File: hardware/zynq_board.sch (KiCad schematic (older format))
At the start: 0 parts

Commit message: WIP: routing the HF Part of the Camera Connector. I have to move the clock away from the left border.
TODO: Fix DDR3 RAM.
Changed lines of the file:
@@
 F1 "pmic.sch" 60
 F2 "PS_POR_B" O R 6500 6700 60
-F3 "V_IN" I R 6500 5950 60
 $EndSheet
 $Sheet
@@
 F0 "DDR" 60
 F1 "ddr.sch" 60
-$EndSheet
-$Sheet
-S 23600 16850 2100 1100
-U 597B38C9
-F0 "10G Clock" 60
-F1 "10G_clock.sch" 60
-F2 "156_25_MHZ_0_P" O L 23600 16950 60
-F3 "156_25_MHZ_0_N" O L 23600 17050 60
-F4 "125_00_MHZ_P" O L 23600 17250 60
-F5 "125_00_MHZ_N" O L 23600 17350 60
-F6 "156_25_MHZ_1_P" O L 23600 17550 60
-F7 "156_25_MHZ_1_N" O L 23600 17650 60
 $EndSheet
 $Sheet
@@
 F13 "CLK" O R 6500 9750 60
 F14 "VBUS_FAULT" O R 6500 10050 60
-F15 "RESETB" I R 6500 9950 60
 $EndSheet
 $Sheet
@@
 F7 "MGTX_RX_1_P" I R 13250 19050 60
 F8 "MGTX_RX_2_P" I R 13250 18950 60
-F9 "MGTREFCLK_0_N" I R 13250 18450 60
-F10 "MGTREFCLK_0_P" I R 13250 18350 60
-F11 "MGTREFCLK_1_N" I R 13250 18700 60
-F12 "MGTREFCLK_1_P" I R 13250 18600 60
-F13 "MGTX_RX_3_P" I R 13250 18850 60
-F14 "MGTX_TX_0_P" O R 13250 20100 60
-F15 "MGTX_TX_1_P" O R 13250 20000 60
-F16 "MGTX_TX_2_P" O R 13250 19900 60
-F17 "MGTX_TX_3_P" O R 13250 19800 60
-F18 "MGTX_TX_0_N" O R 13250 20550 60
-F19 "MGTX_TX_1_N" O R 13250 20450 60
-F20 "MGTX_TX_2_N" O R 13250 20350 60
-F21 "MGTX_TX_3_N" O R 13250 20250 60
+F9 "MGTX_RX_3_P" I R 13250 18850 60
+F10 "MGTX_TX_0_P" O R 13250 20100 60
+F11 "MGTX_TX_1_P" O R 13250 20000 60
+F12 "MGTX_TX_2_P" O R 13250 19900 60
+F13 "MGTX_TX_3_P" O R 13250 19800 60
+F14 "MGTX_TX_0_N" O R 13250 20550 60
+F15 "MGTX_TX_1_N" O R 13250 20450 60
+F16 "MGTX_TX_2_N" O R 13250 20350 60
+F17 "MGTX_TX_3_N" O R 13250 20250 60
 $EndSheet
 $Sheet
@@
 F8 "INA[0]_P" I L 23600 20100 60
 F9 "INA[0]_N" I L 23600 20550 60
-F10 "REFCLK0_P" I L 23600 18550 60
-F11 "REFCLK0_N" I L 23600 18650 60
-F12 "HSRXA_P" I R 25700 18550 60
-F13 "HSRXA_N" I R 25700 18650 60
-F14 "MDC" I R 25700 20950 60
-F15 "LS_OK_IN_A" I R 25700 20550 60
-F16 "LS_OK_OUT_A" O R 25700 20650 60
-F17 "ST" I R 25700 20400 60
-F18 "PRBSEN" I R 25700 20800 60
-F19 "MDIO" B R 25700 21050 60
-F20 "OUTA[3]_P" O L 23600 18850 60
-F21 "OUTA[3]_N" O L 23600 19300 60
-F22 "OUTA[2]_P" O L 23600 18950 60
-F23 "OUTA[2]_N" O L 23600 19400 60
-F24 "OUTA[1]_P" O L 23600 19050 60
-F25 "OUTA[1]_N" O L 23600 19500 60
-F26 "OUTA[0]_P" O L 23600 19150 60
-F27 "OUTA[0]_N" O L 23600 19600 60
-F28 "HSTXA_P" O R 25700 18800 60
-F29 "HSTXA_N" O R 25700 18900 60
-F30 "~TLK_RESET~" I R 25700 21200 60
+F10 "HSRXA_P" I R 25700 18550 60
+F11 "HSRXA_N" I R 25700 18650 60
+F12 "MDC" I R 25700 20950 60
+F13 "LS_OK_IN_A" I R 25700 20550 60
+F14 "LS_OK_OUT_A" O R 25700 20650 60
+F15 "ST" I R 25700 20400 60
+F16 "PRBSEN" I R 25700 20800 60
+F17 "MDIO" B R 25700 21050 60
+F18 "OUTA[3]_P" O L 23600 18850 60
+F19 "OUTA[3]_N" O L 23600 19300 60
+F20 "OUTA[2]_P" O L 23600 18950 60
+F21 "OUTA[2]_N" O L 23600 19400 60
+F22 "OUTA[1]_P" O L 23600 19050 60
+F23 "OUTA[1]_N" O L 23600 19500 60
+F24 "OUTA[0]_P" O L 23600 19150 60
+F25 "OUTA[0]_N" O L 23600 19600 60
+F26 "HSTXA_P" O R 25700 18800 60
+F27 "HSTXA_N" O R 25700 18900 60
 $EndSheet
 $Sheet
@@
 	13450 22250 13450 2650
 Wire Wire Line
-	13250 18350 22700 18350
-Wire Wire Line
-	22700 18350 22700 16950
-Wire Wire Line
-	22700 16950 23600 16950
-Wire Wire Line
-	23600 17050 22800 17050
-Wire Wire Line
-	22800 17050 22800 18450
-Wire Wire Line
-	22800 18450 13250 18450
-Wire Wire Line
-	13250 18600 23000 18600
-Wire Wire Line
-	23000 18600 23000 17250
-Wire Wire Line
-	23000 17250 23600 17250
-Wire Wire Line
-	13250 18700 23100 18700
-Wire Wire Line
-	23100 18700 23100 17350
-Wire Wire Line
-	23100 17350 23600 17350
-Wire Wire Line
-	23600 17550 23500 17550
-Wire Wire Line
-	23500 17550 23500 18550
-Wire Wire Line
-	23500 18550 23600 18550
-Wire Wire Line
-	23600 17650 23400 17650
-Wire Wire Line
-	23400 17650 23400 18650
-Wire Wire Line
-	23400 18650 23600 18650
-Wire Wire Line
 	13250 18850 23600 18850
 Wire Wire Line
@@
 Wire Wire Line
 	25700 21050 26550 21050
-Wire Wire Line
-	25700 21200 26550 21200
 Text Label 26550 20550 2    60   ~ 0
 LS_OK_IN_A
@@
 Text Label 26550 21050 2    60   ~ 0
 MDIO
-Text Label 26550 21200 2    60   ~ 0
-~TLK_RESET~
 Wire Wire Line
 	13250 5100 14100 5100
@@
 Wire Wire Line
 	13250 4600 14100 4600
-Wire Wire Line
-	13250 4500 14100 4500
 Text Label 14100 5000 2    60   ~ 0
 LS_OK_IN_A
@@
 Text Label 14100 4600 2    60   ~ 0
 MDIO
-Text Label 14100 4500 2    60   ~ 0
-~TLK_RESET~
 Wire Wire Line
 	19600 6600 20500 6600
@@
 Text Label 14150 4300 2    60   ~ 0
 IMU_INT2_GPIO2
+Text Label 7200 9950 0    60   ~ 0
+PG
+Wire Wire Line
+	7450 9950 7200 9950
+Text Label 6800 6700 2    60   ~ 0
+PG
+Wire Wire Line
+	6800 6700 6500 6700
+Text Label 13800 8550 2    60   ~ 0
+IMU_MISO
+Wire Wire Line
+	13250 8550 13800 8550
+Text Label 13800 8650 2    60   ~ 0
+IMU_MOSI
+Wire Wire Line
+	13250 8650 13800 8650
+Text Label 13800 8900 2    60   ~ 0
+IMU_EN_0
+Wire Wire Line
+	13250 8900 13800 8900
+Text Label 13800 9000 2    60   ~ 0
+IMU_EN_1
+Wire Wire Line
+	13250 9000 13800 9000
+Text Label 13800 8750 2    60   ~ 0
+IMU_CLK
+Wire Wire Line
+	13250 8750 13800 8750
+Text Label 17350 8550 0    60   ~ 0
+IMU_MISO
+Wire Wire Line
+	17900 8550 17350 8550
+Text Label 17350 8650 0    60   ~ 0
+IMU_MOSI
+Wire Wire Line
+	17900 8650 17350 8650
+Text Label 17350 8900 0    60   ~ 0
+IMU_EN_0
+Wire Wire Line
+	17900 8900 17350 8900
+Text Label 17350 9000 0    60   ~ 0
+IMU_EN_1
+Wire Wire Line
+	17900 9000 17350 9000
+Text Label 17350 8750 0    60   ~ 0
+IMU_CLK
+Wire Wire Line
+	17900 8750 17350 8750
+Text Label 14450 8500 0    60   ~ 0
+LED1
+Text Label 14450 8600 0    60   ~ 0
+LED2
+Wire Wire Line
+	14950 8500 14450 8500
+Wire Wire Line
+	14950 8600 14450 8600
+$Sheet
+S 5000 3200 1500 1150
+U 5AFB0E10
+F0 "Power Connector, Protection" 60
+F1 "pwr_con_fuse_filter.sch" 60
+$EndSheet
 $Sheet
 S 10500 2550 2750 3550
@@
 F18 "TXD" O R 13250 3950 60
 F19 "~SBA~" O R 13250 3650 60
-F20 "~TLK_RESET~" O R 13250 4500 60
-F21 "GPIO_9" B R 13250 2650 60
-F22 "GPIO_10" B R 13250 2750 60
-F23 "GPIO_11" B R 13250 2850 60
-F24 "GPIO_12" B R 13250 2950 60
-F25 "GPIO_13" B R 13250 3050 60
-F26 "GPIO_14" B R 13250 3150 60
-F27 "GPIO_15" B R 13250 3250 60
-F28 "IMU_FRAME_GPIO0" O R 13250 4100 60
-F29 "IMU_INT1_GPIO1" I R 13250 4200 60
-F30 "IMU_INT0_GPIO2" I R 13250 4300 60
-$EndSheet
-Text Label 7200 9950 0    60   ~ 0
-PG
-Wire Wire Line
-	7450 9950 7200 9950
-Text Label 6800 6700 2    60   ~ 0
-PG
-Wire Wire Line
-	6800 6700 6500 6700
-Text Label 13800 8550 2    60   ~ 0
-IMU_MISO
-Wire Wire Line
-	13250 8550 13800 8550
-Text Label 13800 8650 2    60   ~ 0
-IMU_MOSI
-Wire Wire Line
-	13250 8650 13800 8650
-Text Label 13800 8900 2    60   ~ 0
-IMU_EN_0
-Wire Wire Line
-	13250 8900 13800 8900
-Text Label 13800 9000 2    60   ~ 0
-IMU_EN_1
-Wire Wire Line
-	13250 9000 13800 9000
-Text Label 13800 8750 2    60   ~ 0
-IMU_CLK
-Wire Wire Line
-	13250 8750 13800 8750
-Text Label 17350 8550 0    60   ~ 0
-IMU_MISO
-Wire Wire Line
-	17900 8550 17350 8550
-Text Label 17350 8650 0    60   ~ 0
-IMU_MOSI
-Wire Wire Line
-	17900 8650 17350 8650
-Text Label 17350 8900 0    60   ~ 0
-IMU_EN_0
-Wire Wire Line
-	17900 8900 17350 8900
-Text Label 17350 9000 0    60   ~ 0
-IMU_EN_1
-Wire Wire Line
-	17900 9000 17350 9000
-Text Label 17350 8750 0    60   ~ 0
-IMU_CLK
-Wire Wire Line
-	17900 8750 17350 8750
-Text Label 14450 8500 0    60   ~ 0
-LED1
-Text Label 14450 8600 0    60   ~ 0
-LED2
-Wire Wire Line
-	14950 8500 14450 8500
-Wire Wire Line
-	14950 8600 14450 8600
-$Sheet
-S 5000 3200 1500 1150
-U 5AFB0E10
-F0 "Power Connector, Protection" 60
-F1 "pwr_con_fuse_filter.sch" 60
-F2 "V_IN" O R 6500 3800 60
-$EndSheet
-Wire Wire Line
-	6500 3800 6800 3800
-Text Label 6800 3800 2    60   ~ 0
-V_IN
-Wire Wire Line
-	6500 5950 6800 5950
-Text Label 6800 5950 2    60   ~ 0
-V_IN
+F20 "GPIO_9" B R 13250 2650 60
+F21 "GPIO_10" B R 13250 2750 60
+F22 "GPIO_11" B R 13250 2850 60
+F23 "GPIO_12" B R 13250 2950 60
+F24 "GPIO_13" B R 13250 3050 60
+F25 "GPIO_14" B R 13250 3150 60
+F26 "GPIO_15" B R 13250 3250 60
+F27 "IMU_FRAME_GPIO0" O R 13250 4100 60
+F28 "IMU_INT1_GPIO1" I R 13250 4200 60
+F29 "IMU_INT0_GPIO2" I R 13250 4300 60
+$EndSheet
+$Sheet
+S 23600 16850 2100 1100
+U 597B38C9
+F0 "10G Clock" 60
+F1 "10G_clock.sch" 60
+$EndSheet
 $EndSCHEMATC

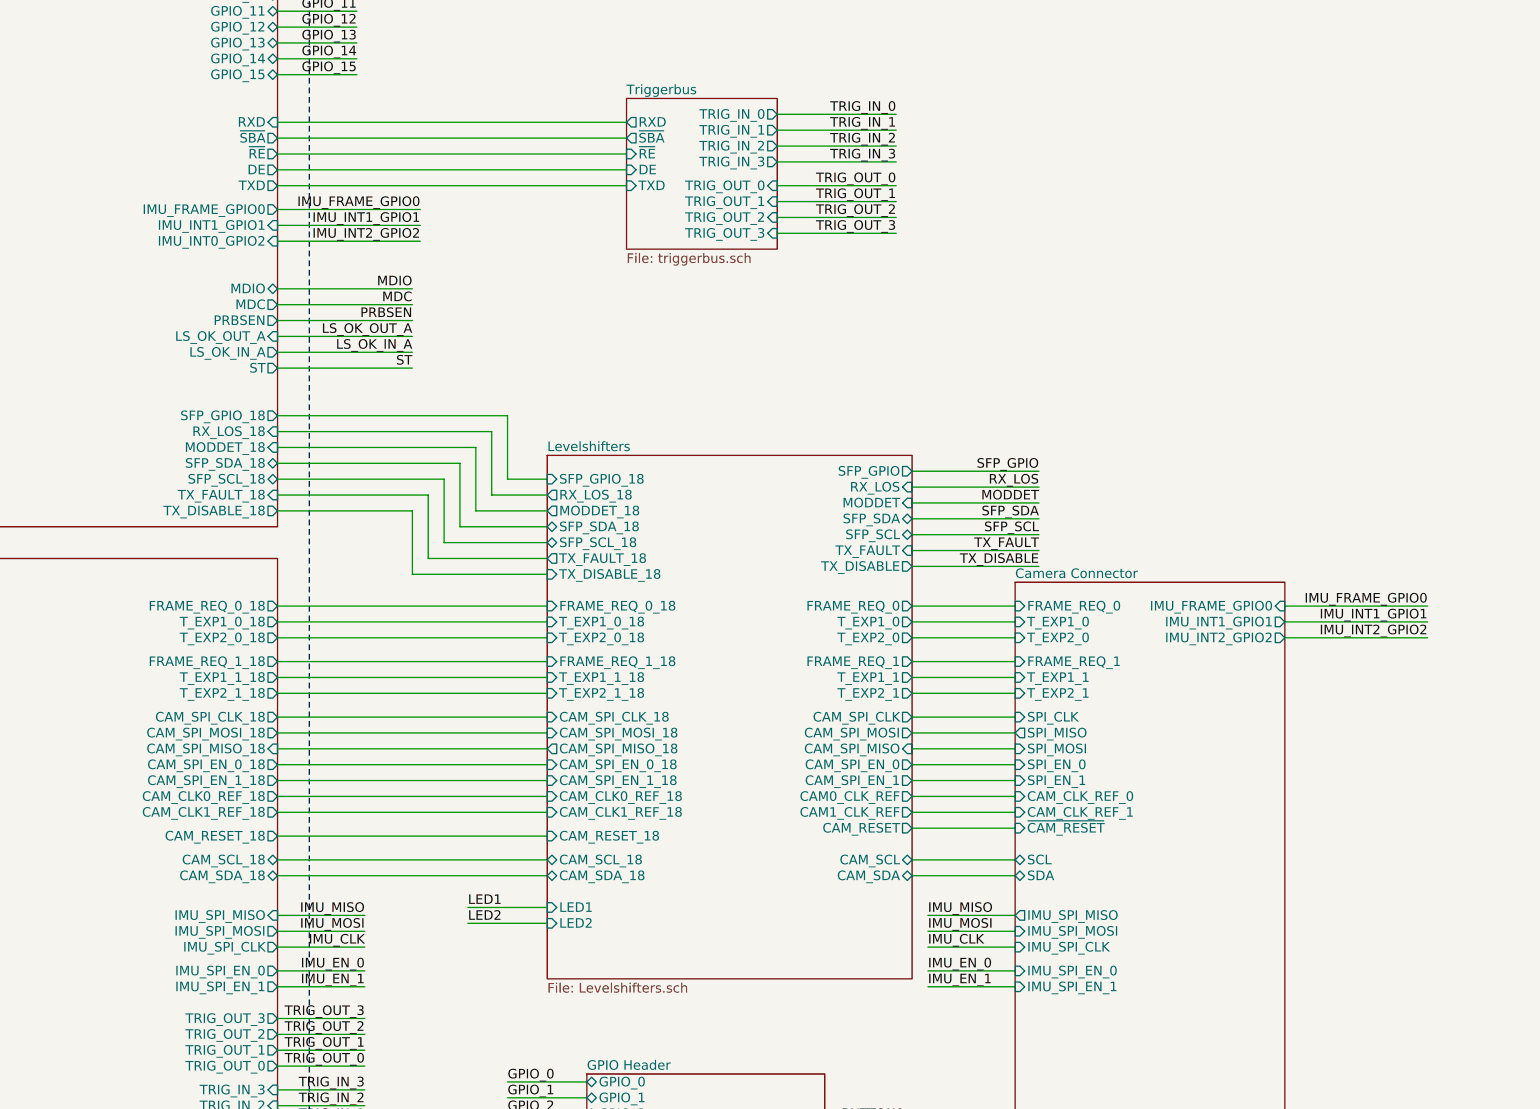
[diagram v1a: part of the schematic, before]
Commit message: Added Courtyard to selfmade Footprints. Also general Routing WIP.
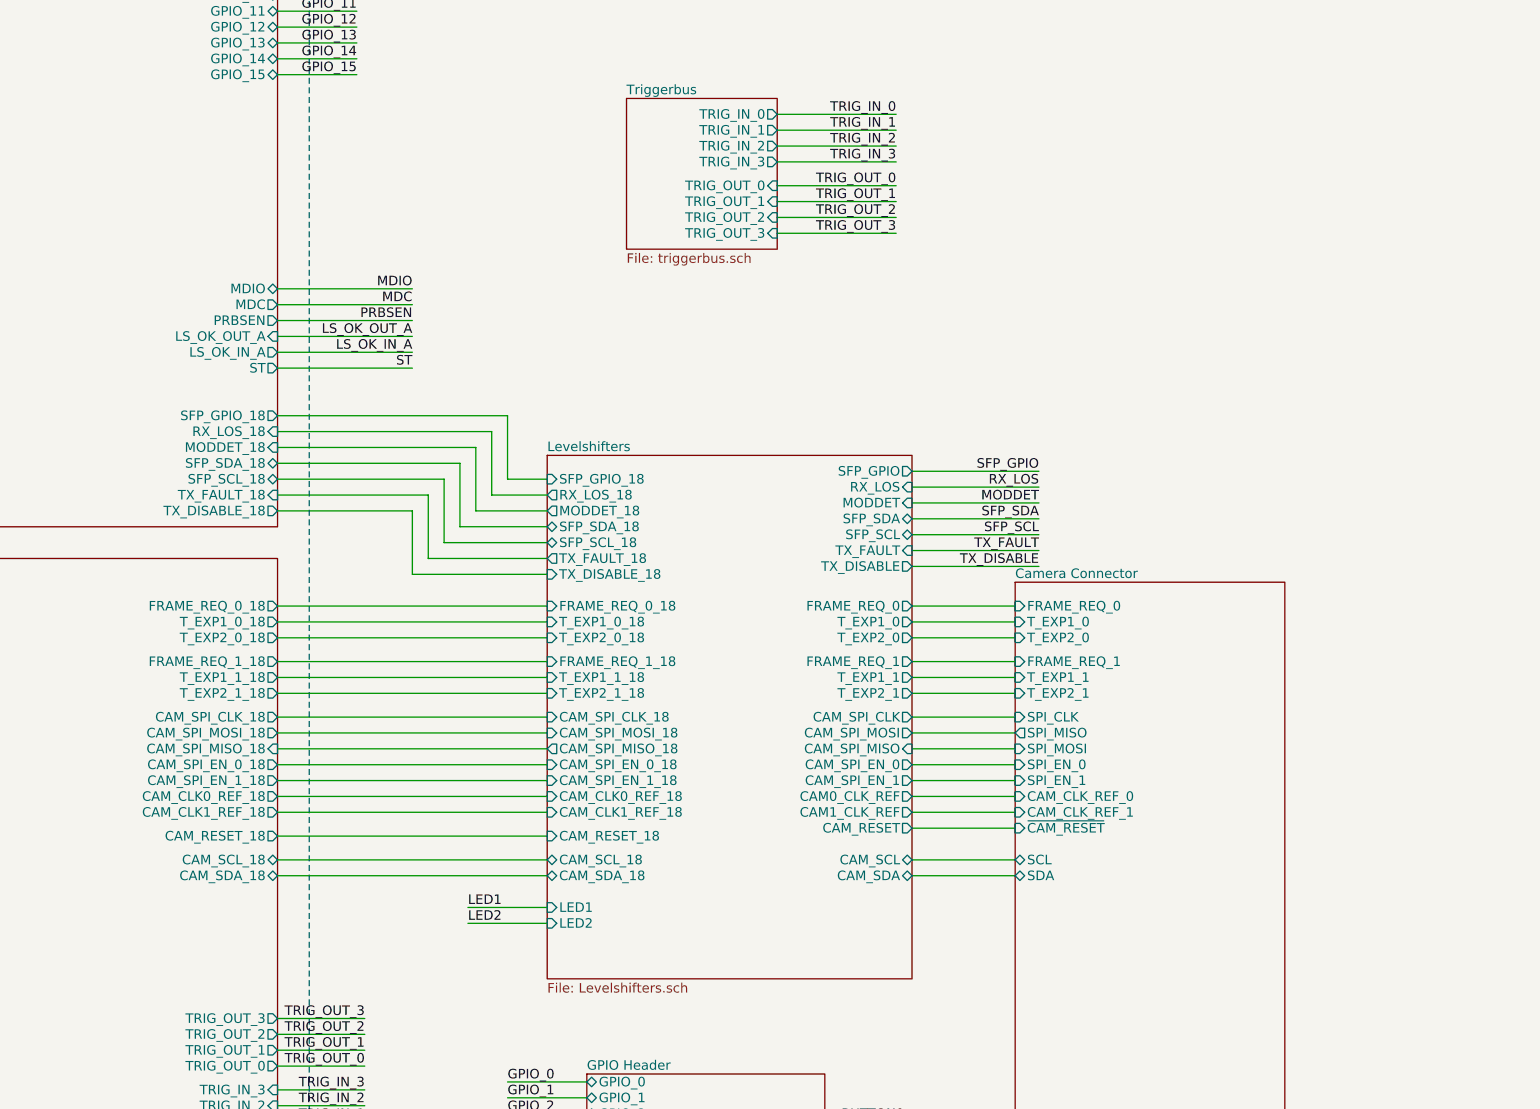
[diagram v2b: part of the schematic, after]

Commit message: WIP: general Routing
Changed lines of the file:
@@
 F21 "CAM_RESET" O R 17250 8000 60
 F22 "CAM_SPI_EN_0" O R 17250 7600 60
-F23 "CAM_SCL_18" B L 14950 8200 60
-F24 "CAM_SDA_18" B L 14950 8300 60
-F25 "SFP_SCL_18" B L 14950 6200 60
-F26 "SFP_SDA_18" B L 14950 6100 60
-F27 "CAM_RESET_18" I L 14950 8050 60
-F28 "CAM_SPI_EN_1_18" I L 14950 7700 60
-F29 "CAM_SPI_EN_0_18" I L 14950 7600 60
-F30 "CAM_SPI_MOSI_18" I L 14950 7400 60
-F31 "CAM_SPI_CLK_18" I L 14950 7300 60
-F32 "T_EXP2_1_18" I L 14950 7150 60
-F33 "T_EXP1_1_18" I L 14950 7050 60
-F34 "FRAME_REQ_1_18" I L 14950 6950 60
-F35 "T_EXP2_0_18" I L 14950 6800 60
-F36 "T_EXP1_0_18" I L 14950 6700 60
-F37 "FRAME_REQ_0_18" I L 14950 6600 60
-F38 "CAM_SPI_MISO_18" O L 14950 7500 60
-F39 "RX_LOS_18" O L 14950 5900 60
-F40 "TX_FAULT_18" O L 14950 6300 60
-F41 "MODDET_18" O L 14950 6000 60
-F42 "SFP_GPIO_18" I L 14950 5800 60
-F43 "TX_DISABLE_18" I L 14950 6400 60
-F44 "CAM1_CLK_REF" O R 17250 7900 60
-F45 "CAM_CLK1_REF_18" I L 14950 7900 60
-F46 "CAM_CLK0_REF_18" I L 14950 7800 60
-F47 "CAM0_CLK_REF" O R 17250 7800 60
-F48 "LED1" I L 14950 8500 60
-F49 "LED2" I L 14950 8600 60
+F23 "SFP_SCL_18" B L 14950 6200 60
+F24 "SFP_SDA_18" B L 14950 6100 60
+F25 "CAM_RESET_18" I L 14950 8050 60
+F26 "CAM_SPI_EN_1_18" I L 14950 7700 60
+F27 "CAM_SPI_EN_0_18" I L 14950 7600 60
+F28 "CAM_SPI_MOSI_18" I L 14950 7400 60
+F29 "CAM_SPI_CLK_18" I L 14950 7300 60
+F30 "T_EXP2_1_18" I L 14950 7150 60
+F31 "T_EXP1_1_18" I L 14950 7050 60
+F32 "FRAME_REQ_1_18" I L 14950 6950 60
+F33 "T_EXP2_0_18" I L 14950 6800 60
+F34 "T_EXP1_0_18" I L 14950 6700 60
+F35 "FRAME_REQ_0_18" I L 14950 6600 60
+F36 "CAM_SPI_MISO_18" O L 14950 7500 60
+F37 "RX_LOS_18" O L 14950 5900 60
+F38 "TX_FAULT_18" O L 14950 6300 60
+F39 "MODDET_18" O L 14950 6000 60
+F40 "SFP_GPIO_18" I L 14950 5800 60
+F41 "TX_DISABLE_18" I L 14950 6400 60
+F42 "CAM1_CLK_REF" O R 17250 7900 60
+F43 "CAM_CLK1_REF_18" I L 14950 7900 60
+F44 "CAM_CLK0_REF_18" I L 14950 7800 60
+F45 "CAM0_CLK_REF" O R 17250 7800 60
+F46 "LED1" I L 14950 8500 60
+F47 "LED2" I L 14950 8600 60
 $EndSheet
 $Sheet
@@
 Text Label 17150 3800 2    60   ~ 0
 TRIG_IN_3
-Text Label 13750 10100 2    60   ~ 0
-GPIO_0
-Text Label 13750 10200 2    60   ~ 0
-GPIO_1
-Text Label 13750 10300 2    60   ~ 0
-GPIO_2
-Text Label 13750 10400 2    60   ~ 0
-GPIO_3
-Text Label 13750 10500 2    60   ~ 0
-GPIO_4
-Text Label 13750 10600 2    60   ~ 0
-GPIO_5
-Text Label 13750 10700 2    60   ~ 0
-GPIO_6
-Text Label 13750 10800 2    60   ~ 0
-GPIO_7
-Text Label 13750 10900 2    60   ~ 0
-GPIO_8
 Text Label 13750 3250 2    60   ~ 0
 GPIO_15
@@
 Wire Wire Line
 	13250 8050 14950 8050
-Wire Wire Line
-	14950 8200 13250 8200
-Wire Wire Line
-	13250 8300 14950 8300
 Wire Notes Line
 	13450 2350 7250 2350
@@
 Wire Wire Line
 	13250 3250 13750 3250
-Wire Wire Line
-	13250 10100 13750 10100
-Wire Wire Line
-	13250 10200 13750 10200
-Wire Wire Line
-	13250 10300 13750 10300
-Wire Wire Line
-	13250 10400 13750 10400
-Wire Wire Line
-	13250 10500 13750 10500
-Wire Wire Line
-	13250 10600 13750 10600
-Wire Wire Line
-	13250 10700 13750 10700
-Wire Wire Line
-	13250 10800 13750 10800
-Wire Wire Line
-	13250 10900 13750 10900
-$Sheet
-S 15200 9550 1500 1700
-U 5B0F4BF9
-F0 "GPIO Header" 60
-F1 "gpio.sch" 60
-F2 "GPIO_0" B L 15200 9600 60
-F3 "GPIO_1" B L 15200 9700 60
-F4 "GPIO_2" B L 15200 9800 60
-F5 "GPIO_3" B L 15200 9900 60
-F6 "GPIO_4" B L 15200 10000 60
-F7 "GPIO_5" B L 15200 10100 60
-F8 "GPIO_6" B L 15200 10200 60
-F9 "GPIO_7" B L 15200 10300 60
-F10 "GPIO_8" B L 15200 10400 60
-F11 "GPIO_9" B L 15200 10500 60
-F12 "GPIO_10" B L 15200 10600 60
-F13 "GPIO_11" B L 15200 10700 60
-F14 "GPIO_12" B L 15200 10800 60
-F15 "GPIO_13" B L 15200 10900 60
-F16 "GPIO_14" B L 15200 11000 60
-F17 "GPIO_15" B L 15200 11100 60
-F18 "BUTTON1" O R 16700 9850 60
-$EndSheet
-Text Label 14700 9600 0    60   ~ 0
-GPIO_0
-Wire Wire Line
-	14700 9600 15200 9600
-Text Label 14700 9700 0    60   ~ 0
-GPIO_1
-Wire Wire Line
-	14700 9700 15200 9700
-Text Label 14700 9800 0    60   ~ 0
-GPIO_2
-Wire Wire Line
-	14700 9800 15200 9800
-Text Label 14700 9900 0    60   ~ 0
-GPIO_3
-Wire Wire Line
-	14700 9900 15200 9900
-Text Label 14700 10000 0    60   ~ 0
-GPIO_4
-Wire Wire Line
-	14700 10000 15200 10000
-Text Label 14700 10100 0    60   ~ 0
-GPIO_5
-Wire Wire Line
-	14700 10100 15200 10100
-Text Label 14700 10200 0    60   ~ 0
-GPIO_6
-Wire Wire Line
-	14700 10200 15200 10200
-Text Label 14700 10300 0    60   ~ 0
-GPIO_7
-Wire Wire Line
-	14700 10300 15200 10300
-Text Label 14700 10400 0    60   ~ 0
-GPIO_8
-Wire Wire Line
-	14700 10400 15200 10400
-Text Label 14700 10500 0    60   ~ 0
-GPIO_9
-Wire Wire Line
-	14700 10500 15200 10500
-Text Label 14700 10600 0    60   ~ 0
-GPIO_10
-Wire Wire Line
-	14700 10600 15200 10600
-Text Label 14700 10700 0    60   ~ 0
-GPIO_11
-Wire Wire Line
-	14700 10700 15200 10700
-Text Label 14700 10800 0    60   ~ 0
-GPIO_12
-Wire Wire Line
-	14700 10800 15200 10800
-Text Label 14700 10900 0    60   ~ 0
-GPIO_13
-Wire Wire Line
-	14700 10900 15200 10900
-Text Label 14700 11000 0    60   ~ 0
-GPIO_14
-Wire Wire Line
-	14700 11000 15200 11000
-Text Label 14700 11100 0    60   ~ 0
-GPIO_15
-Wire Wire Line
-	14700 11100 15200 11100
 Text Label 13750 11150 2    60   ~ 0
 LED1
@@
 F12 "CAM_SPI_EN_0_18" O R 13250 7600 60
 F13 "CAM_RESET_18" O R 13250 8050 60
-F14 "CAM_SCL_18" B R 13250 8200 60
-F15 "CAM_SDA_18" B R 13250 8300 60
-F16 "TRIG_IN_0" I R 13250 9950 60
-F17 "TRIG_IN_1" I R 13250 9850 60
-F18 "TRIG_IN_2" I R 13250 9750 60
-F19 "TRIG_IN_3" I R 13250 9650 60
-F20 "TRIG_OUT_0" O R 13250 9500 60
-F21 "TRIG_OUT_2" O R 13250 9300 60
-F22 "TRIG_OUT_1" O R 13250 9400 60
-F23 "TRIG_OUT_3" O R 13250 9200 60
-F24 "GPIO_0" B R 13250 10100 60
-F25 "GPIO_1" B R 13250 10200 60
-F26 "GPIO_2" B R 13250 10300 60
-F27 "GPIO_3" B R 13250 10400 60
-F28 "GPIO_4" B R 13250 10500 60
-F29 "GPIO_5" B R 13250 10600 60
-F30 "GPIO_6" B R 13250 10700 60
-F31 "GPIO_7" B R 13250 10800 60
-F32 "GPIO_8" B R 13250 10900 60
-F33 "LED1" O R 13250 11150 60
-F34 "LED2" O R 13250 11250 60
-F35 "BUTTON0" I R 13250 11350 60
-F36 "CAM_CLK0_REF_18" O R 13250 7800 60
-F37 "CAM_CLK1_REF_18" O R 13250 7900 60
+F14 "TRIG_IN_0" I R 13250 9950 60
+F15 "TRIG_IN_1" I R 13250 9850 60
+F16 "TRIG_IN_2" I R 13250 9750 60
+F17 "TRIG_IN_3" I R 13250 9650 60
+F18 "TRIG_OUT_0" O R 13250 9500 60
+F19 "TRIG_OUT_2" O R 13250 9300 60
+F20 "TRIG_OUT_1" O R 13250 9400 60
+F21 "TRIG_OUT_3" O R 13250 9200 60
+F22 "LED1" O R 13250 11150 60
+F23 "LED2" O R 13250 11250 60
+F24 "BUTTON0" I R 13250 11350 60
+F25 "CAM_CLK0_REF_18" O R 13250 7800 60
+F26 "CAM_CLK1_REF_18" O R 13250 7900 60
+$EndSheet
+$Sheet
+S 15200 9550 1500 1700
+U 5B0F4BF9
+F0 "GPIO Header" 60
+F1 "gpio.sch" 60
+F2 "BUTTON1" O R 16700 9850 60
 $EndSheet
 $EndSCHEMATC
